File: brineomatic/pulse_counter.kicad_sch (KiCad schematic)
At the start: 6 parts, among them J1 Conn_01x03

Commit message: starting to shape up, footprints etc
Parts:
- C2: footprint (none) -> Capacitor_SMD:C_0805_2012Metric_Pad1.18x1.45mm_HandSolder
- J2: renamed from J1; footprint (none) -> TerminalBlock_Phoenix:TerminalBlock_Phoenix_PT-1,5-3-3.5-H_1x03_P3.50mm_Horizontal
- R5: renamed from R4; footprint (none) -> Resistor_SMD:R_0805_2012Metric_Pad1.20x1.40mm_HandSolder
- R6: renamed from R5; footprint (none) -> Resistor_SMD:R_0805_2012Metric_Pad1.20x1.40mm_HandSolder
- R7: renamed from R3; footprint (none) -> Resistor_SMD:R_0805_2012Metric_Pad1.20x1.40mm_HandSolder
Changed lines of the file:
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@@
 		(dnp no)
 		(fields_autoplaced yes)
-		(property "Reference" "#PWR04"
+		(property "Reference" "#PWR010"
 			(at 105.41 120.65 0)
 			(effects
@@
 			(project ""
 				(path "/96477ae2-ef08-48f3-8dd4-fe4478541f68/afb25a63-7dc0-4ba4-a0ca-4f0b83c59f3b"
-					(reference "#PWR04")
+					(reference "#PWR010")
 					(unit 1)
 				)
@@
 		(dnp no)
 		(fields_autoplaced yes)
-		(property "Reference" "#PWR03"
+		(property "Reference" "#PWR09"
 			(at 105.41 97.79 0)
 			(effects
@@
 			(project ""
 				(path "/96477ae2-ef08-48f3-8dd4-fe4478541f68/afb25a63-7dc0-4ba4-a0ca-4f0b83c59f3b"
-					(reference "#PWR03")
+					(reference "#PWR09")
 					(unit 1)
 				)
@@
 		(on_board yes)
 		(dnp no)
-		(property "Reference" "R3"
+		(property "Reference" "R7"
 			(at 135.89 99.06 90)
 			(effects
@@
 			)
 		)
-		(property "Footprint" ""
+		(property "Footprint" "Resistor_SMD:R_0805_2012Metric_Pad1.20x1.40mm_HandSolder"
 			(at 135.89 104.14 0)
 			(effects
@@
 			(project ""
 				(path "/96477ae2-ef08-48f3-8dd4-fe4478541f68/afb25a63-7dc0-4ba4-a0ca-4f0b83c59f3b"
-					(reference "R3")
+					(reference "R7")
 					(unit 1)
 				)
@@
 		(dnp no)
 		(fields_autoplaced yes)
-		(property "Reference" "J1"
+		(property "Reference" "J2"
 			(at 100.33 95.25 0)
 			(effects
@@
 			)
 		)
-		(property "Footprint" ""
+		(property "Footprint" "TerminalBlock_Phoenix:TerminalBlock_Phoenix_PT-1,5-3-3.5-H_1x03_P3.50mm_Horizontal"
 			(at 100.33 104.14 0)
 			(effects
@@
 			(project ""
 				(path "/96477ae2-ef08-48f3-8dd4-fe4478541f68/afb25a63-7dc0-4ba4-a0ca-4f0b83c59f3b"
-					(reference "J1")
+					(reference "J2")
 					(unit 1)
 				)
@@
 		(dnp no)
 		(fields_autoplaced yes)
-		(property "Reference" "R4"
+		(property "Reference" "R5"
 			(at 125.73 99.0599 0)
 			(effects
@@
 			)
 		)
-		(property "Footprint" ""
+		(property "Footprint" "Resistor_SMD:R_0805_2012Metric_Pad1.20x1.40mm_HandSolder"
 			(at 123.19 100.33 0)
 			(effects
@@
 			(project "brineomatic"
 				(path "/96477ae2-ef08-48f3-8dd4-fe4478541f68/afb25a63-7dc0-4ba4-a0ca-4f0b83c59f3b"
-					(reference "R4")
+					(reference "R5")
 					(unit 1)
 				)
@@
 			)
 		)
-		(property "Footprint" ""
+		(property "Footprint" "Capacitor_SMD:C_0805_2012Metric_Pad1.18x1.45mm_HandSolder"
 			(at 142.24 107.95 0)
 			(effects
@@
 		(dnp no)
 		(fields_autoplaced yes)
-		(property "Reference" "R5"
+		(property "Reference" "R6"
 			(at 125.73 106.6799 0)
 			(effects
@@
 			)
 		)
-		(property "Footprint" ""
+		(property "Footprint" "Resistor_SMD:R_0805_2012Metric_Pad1.20x1.40mm_HandSolder"
 			(at 123.19 107.95 0)
 			(effects
@@
 			(project "brineomatic"
 				(path "/96477ae2-ef08-48f3-8dd4-fe4478541f68/afb25a63-7dc0-4ba4-a0ca-4f0b83c59f3b"
-					(reference "R5")
-					(unit 1)
-				)
+					(reference "R6")
+					(unit 1)
+				)

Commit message: starting to look good.
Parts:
- J2: value Conn_01x03 -> FLOWMETER; footprint TerminalBlock_Phoenix:TerminalBlock_Phoenix_PT-1,5-3-3.5-H_1x03_P3.50mm_Horizontal -> Connector_JST:JST_PH_S3B-PH-K_1x03_P2.00mm_Horizontal; LCSC (none) -> C7470117
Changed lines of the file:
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@@
 			)
 		)
-		(property "Value" "Conn_01x03"
+		(property "Value" "FLOWMETER"
 			(at 100.33 97.79 0)
 			(effects
@@
 			)
 		)
-		(property "Footprint" "TerminalBlock_Phoenix:TerminalBlock_Phoenix_PT-1,5-3-3.5-H_1x03_P3.50mm_Horizontal"
+		(property "Footprint" "Connector_JST:JST_PH_S3B-PH-K_1x03_P2.00mm_Horizontal"
 			(at 100.33 104.14 0)
 			(effects
@@
 			(at 100.33 104.14 0)
 			(effects
+				(font
+					(size 1.27 1.27)
+				)
+				(hide yes)
+			)
+		)
+		(property "LCSC" "C7470117"
+			(at 100.33 104.14 0)
+			(effects

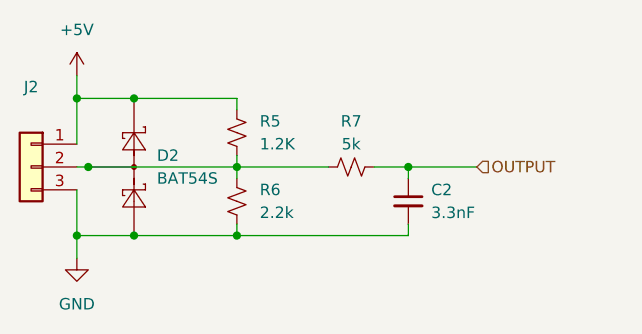
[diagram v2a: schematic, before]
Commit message: updated bom and prepping for Rev A
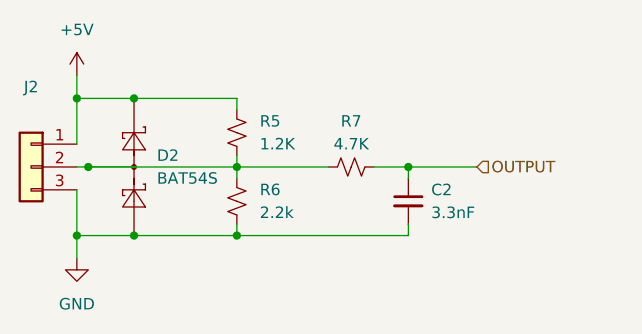
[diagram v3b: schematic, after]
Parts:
- C2: LCSC (none) -> C107149
- J2: value FLOWMETER -> ~; LCSC C7470117 -> C157929
- R5: LCSC (none) -> C114526
- R6: LCSC (none) -> C114561
- R7: value 5k -> 4.7K; LCSC (none) -> C60816
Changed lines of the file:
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@@
 			)
 		)
-		(property "Value" "5k"
+		(property "Value" "4.7K"
 			(at 135.89 101.6 90)
 			(effects
@@
 		)
 		(property "Description" "Resistor, small US symbol"
+			(at 135.89 104.14 0)
+			(effects
+				(font
+					(size 1.27 1.27)
+				)
+				(hide yes)
+			)
+		)
+		(property "LCSC" "C60816"
 			(at 135.89 104.14 0)
 			(effects
@@
 			)
 		)
-		(property "Value" "FLOWMETER"
+		(property "Value" "~"
 			(at 100.33 97.79 0)
 			(effects
@@
 			)
 		)
-		(property "LCSC" "C7470117"
+		(property "LCSC" "C157929"
 			(at 100.33 104.14 0)
 			(effects
@@
 			)
 		)
+		(property "LCSC" "C114526"
+			(at 123.19 100.33 0)
+			(effects
+				(font
+					(size 1.27 1.27)
+				)
+				(hide yes)
+			)
+		)
 		(pin "1"
 		)
@@
 			)
 		)
+		(property "LCSC" "C107149"
+			(at 142.24 107.95 0)
+			(effects
+				(font
+					(size 1.27 1.27)
+				)
+				(hide yes)
+			)
+		)
 		(pin "1"
 		)
@@
 			(at 123.19 107.95 0)
 			(effects
+				(font
+					(size 1.27 1.27)
+				)
+				(hide yes)
+			)
+		)
+		(property "LCSC" "C114561"
+			(at 123.19 107.95 0)
+			(effects

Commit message: fixed bat54s placement.
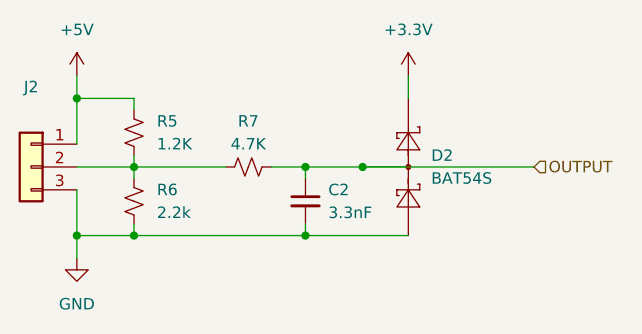
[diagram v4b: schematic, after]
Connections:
- net +5V: no longer D2.2 (K)
- net OUTPUT: now also D2.3 (COM)
- net at J2.2 (Pin_2), R5.1, R6.2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: no longer D2.3 (COM)
- new net +3.3V: D2.2 (K)
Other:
- moved on the sheet: C2, D2, R5, R6, R7

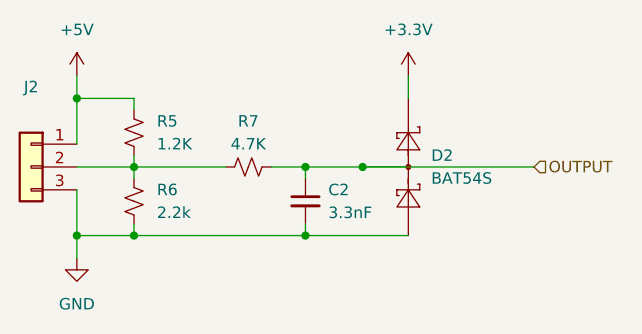
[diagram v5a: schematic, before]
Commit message: did a bunch of schematic work for Rev B
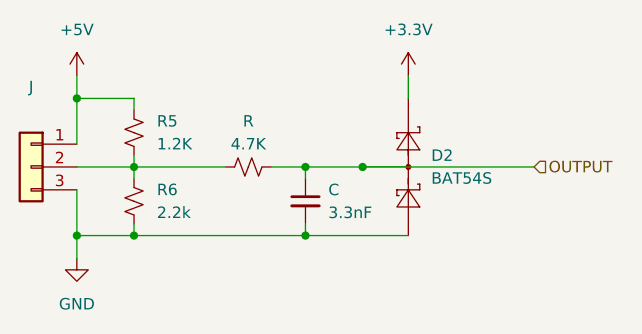
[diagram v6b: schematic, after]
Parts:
- renumbered C2 to C, J2 to J, R7 to R
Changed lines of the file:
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@@
 		(dnp no)
 		(fields_autoplaced yes)
-		(property "Reference" "#PWR010"
+		(property "Reference" "#PWR"
 			(at 105.41 120.65 0)
 			(effects
@@
 		)
 		(instances
-			(project ""
-				(path "/96477ae2-ef08-48f3-8dd4-fe4478541f68/afb25a63-7dc0-4ba4-a0ca-4f0b83c59f3b"
-					(reference "#PWR010")
+			(project "brineomatic"
+				(path "/96477ae2-ef08-48f3-8dd4-fe4478541f68/c28d9395-3f2f-46b5-bdab-c14b6c7c5c4b"
+					(reference "#PWR040")
 					(unit 1)
 				)
@@
 		(dnp no)
 		(fields_autoplaced yes)
-		(property "Reference" "#PWR027"
+		(property "Reference" "#PWR"
 			(at 142.24 97.79 0)
 			(effects
@@
 		)
 		(instances
-			(project ""
-				(path "/96477ae2-ef08-48f3-8dd4-fe4478541f68/afb25a63-7dc0-4ba4-a0ca-4f0b83c59f3b"
-					(reference "#PWR027")
+			(project "brineomatic"
+				(path "/96477ae2-ef08-48f3-8dd4-fe4478541f68/c28d9395-3f2f-46b5-bdab-c14b6c7c5c4b"
+					(reference "#PWR043")
 					(unit 1)
 				)
@@
 		(dnp no)
 		(fields_autoplaced yes)
-		(property "Reference" "#PWR09"
+		(property "Reference" "#PWR"
 			(at 105.41 97.79 0)
 			(effects
@@
 		)
 		(instances
-			(project ""
-				(path "/96477ae2-ef08-48f3-8dd4-fe4478541f68/afb25a63-7dc0-4ba4-a0ca-4f0b83c59f3b"
-					(reference "#PWR09")
+			(project "brineomatic"
+				(path "/96477ae2-ef08-48f3-8dd4-fe4478541f68/c28d9395-3f2f-46b5-bdab-c14b6c7c5c4b"
+					(reference "#PWR039")
 					(unit 1)
 				)
@@
 		(on_board yes)
 		(dnp no)
-		(property "Reference" "R7"
+		(property "Reference" "R"
 			(at 124.46 99.06 90)
 			(effects
@@
 		)
 		(instances
-			(project ""
-				(path "/96477ae2-ef08-48f3-8dd4-fe4478541f68/afb25a63-7dc0-4ba4-a0ca-4f0b83c59f3b"
-					(reference "R7")
+			(project "brineomatic"
+				(path "/96477ae2-ef08-48f3-8dd4-fe4478541f68/c28d9395-3f2f-46b5-bdab-c14b6c7c5c4b"
+					(reference "R14")
 					(unit 1)
 				)
@@
 		(dnp no)
 		(fields_autoplaced yes)
-		(property "Reference" "J2"
+		(property "Reference" "J"
 			(at 100.33 95.25 0)
 			(effects
@@
 		)
 		(instances
-			(project ""
-				(path "/96477ae2-ef08-48f3-8dd4-fe4478541f68/afb25a63-7dc0-4ba4-a0ca-4f0b83c59f3b"
-					(reference "J2")
+			(project "brineomatic"
+				(path "/96477ae2-ef08-48f3-8dd4-fe4478541f68/c28d9395-3f2f-46b5-bdab-c14b6c7c5c4b"
+					(reference "J20")
 					(unit 1)
 				)
@@
 					(unit 1)
 				)
+				(path "/96477ae2-ef08-48f3-8dd4-fe4478541f68/c28d9395-3f2f-46b5-bdab-c14b6c7c5c4b"
+					(reference "D11")
+					(unit 1)
+				)
 			)
 		)
@@
 					(unit 1)
 				)
+				(path "/96477ae2-ef08-48f3-8dd4-fe4478541f68/c28d9395-3f2f-46b5-bdab-c14b6c7c5c4b"
+					(reference "R9")
+					(unit 1)
+				)
 			)
 		)
@@
 		(dnp no)
 		(fields_autoplaced yes)
-		(property "Reference" "C2"
+		(property "Reference" "C"
 			(at 133.35 106.6862 0)
 			(effects
@@
 		)
 		(instances
-			(project ""
-				(path "/96477ae2-ef08-48f3-8dd4-fe4478541f68/afb25a63-7dc0-4ba4-a0ca-4f0b83c59f3b"
-					(reference "C2")
+			(project "brineomatic"
+				(path "/96477ae2-ef08-48f3-8dd4-fe4478541f68/c28d9395-3f2f-46b5-bdab-c14b6c7c5c4b"
+					(reference "C18")
 					(unit 1)
 				)
@@
 					(unit 1)
 				)
+				(path "/96477ae2-ef08-48f3-8dd4-fe4478541f68/c28d9395-3f2f-46b5-bdab-c14b6c7c5c4b"
+					(reference "R10")
+					(unit 1)
+				)

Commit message: worked on schematic and layout a bit more.
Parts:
- C9: renamed from C; footprint Capacitor_SMD:C_0805_2012Metric_Pad1.18x1.45mm_HandSolder -> Capacitor_SMD:C_0603_1608Metric
- R5, R6: footprint Resistor_SMD:R_0805_2012Metric_Pad1.20x1.40mm_HandSolder -> Resistor_SMD:R_0603_1608Metric
- R7: renamed from R; footprint Resistor_SMD:R_0805_2012Metric_Pad1.20x1.40mm_HandSolder -> Resistor_SMD:R_0603_1608Metric
- renumbered J to J2
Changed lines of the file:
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@@
 		(dnp no)
 		(fields_autoplaced yes)
-		(property "Reference" "#PWR"
+		(property "Reference" "#PWR0101"
 			(at 105.41 120.65 0)
 			(effects
@@
 		(instances
 			(project "brineomatic"
+				(path "/96477ae2-ef08-48f3-8dd4-fe4478541f68/afb25a63-7dc0-4ba4-a0ca-4f0b83c59f3b"
+					(reference "#PWR0101")
+					(unit 1)
+				)
 				(path "/96477ae2-ef08-48f3-8dd4-fe4478541f68/c28d9395-3f2f-46b5-bdab-c14b6c7c5c4b"
 					(reference "#PWR040")
@@
 		(dnp no)
 		(fields_autoplaced yes)
-		(property "Reference" "#PWR"
+		(property "Reference" "#PWR0103"
 			(at 142.24 97.79 0)
 			(effects
@@
 		(instances
 			(project "brineomatic"
+				(path "/96477ae2-ef08-48f3-8dd4-fe4478541f68/afb25a63-7dc0-4ba4-a0ca-4f0b83c59f3b"
+					(reference "#PWR0103")
+					(unit 1)
+				)
 				(path "/96477ae2-ef08-48f3-8dd4-fe4478541f68/c28d9395-3f2f-46b5-bdab-c14b6c7c5c4b"
 					(reference "#PWR043")
@@
 		(dnp no)
 		(fields_autoplaced yes)
-		(property "Reference" "#PWR"
+		(property "Reference" "#PWR0102"
 			(at 105.41 97.79 0)
 			(effects
@@
 		(instances
 			(project "brineomatic"
+				(path "/96477ae2-ef08-48f3-8dd4-fe4478541f68/afb25a63-7dc0-4ba4-a0ca-4f0b83c59f3b"
+					(reference "#PWR0102")
+					(unit 1)
+				)
 				(path "/96477ae2-ef08-48f3-8dd4-fe4478541f68/c28d9395-3f2f-46b5-bdab-c14b6c7c5c4b"
 					(reference "#PWR039")
@@
 		(on_board yes)
 		(dnp no)
-		(property "Reference" "R"
+		(property "Reference" "R7"
 			(at 124.46 99.06 90)
 			(effects
@@
 			)
 		)
-		(property "Footprint" "Resistor_SMD:R_0805_2012Metric_Pad1.20x1.40mm_HandSolder"
+		(property "Footprint" "Resistor_SMD:R_0603_1608Metric"
 			(at 124.46 104.14 0)
 			(effects
@@
 		(instances
 			(project "brineomatic"
+				(path "/96477ae2-ef08-48f3-8dd4-fe4478541f68/afb25a63-7dc0-4ba4-a0ca-4f0b83c59f3b"
+					(reference "R7")
+					(unit 1)
+				)
 				(path "/96477ae2-ef08-48f3-8dd4-fe4478541f68/c28d9395-3f2f-46b5-bdab-c14b6c7c5c4b"
 					(reference "R14")
@@
 		(dnp no)
 		(fields_autoplaced yes)
-		(property "Reference" "J"
+		(property "Reference" "J2"
 			(at 100.33 95.25 0)
 			(effects
@@
 		(instances
 			(project "brineomatic"
+				(path "/96477ae2-ef08-48f3-8dd4-fe4478541f68/afb25a63-7dc0-4ba4-a0ca-4f0b83c59f3b"
+					(reference "J2")
+					(unit 1)
+				)
 				(path "/96477ae2-ef08-48f3-8dd4-fe4478541f68/c28d9395-3f2f-46b5-bdab-c14b6c7c5c4b"
 					(reference "J20")
@@
 			)
 		)
-		(property "Footprint" "Resistor_SMD:R_0805_2012Metric_Pad1.20x1.40mm_HandSolder"
+		(property "Footprint" "Resistor_SMD:R_0603_1608Metric"
 			(at 111.76 100.33 0)
 			(effects
@@
 		(dnp no)
 		(fields_autoplaced yes)
-		(property "Reference" "C"
+		(property "Reference" "C9"
 			(at 133.35 106.6862 0)
 			(effects
@@
 			)
 		)
-		(property "Footprint" "Capacitor_SMD:C_0805_2012Metric_Pad1.18x1.45mm_HandSolder"
+		(property "Footprint" "Capacitor_SMD:C_0603_1608Metric"
 			(at 130.81 107.95 0)
 			(effects
@@
 		(instances
 			(project "brineomatic"
+				(path "/96477ae2-ef08-48f3-8dd4-fe4478541f68/afb25a63-7dc0-4ba4-a0ca-4f0b83c59f3b"
+					(reference "C9")
+					(unit 1)
+				)
 				(path "/96477ae2-ef08-48f3-8dd4-fe4478541f68/c28d9395-3f2f-46b5-bdab-c14b6c7c5c4b"
 					(reference "C18")
@@
 			)
 		)
-		(property "Footprint" "Resistor_SMD:R_0805_2012Metric_Pad1.20x1.40mm_HandSolder"
+		(property "Footprint" "Resistor_SMD:R_0603_1608Metric"
 			(at 111.76 107.95 0)
 			(effects

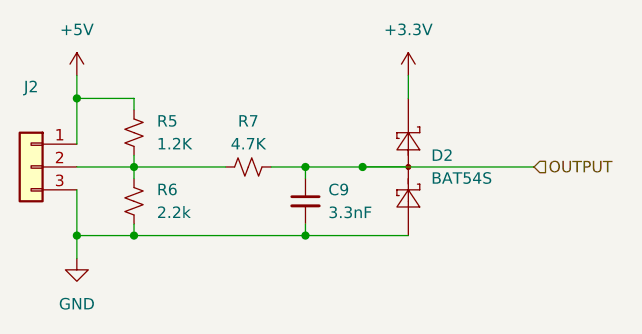
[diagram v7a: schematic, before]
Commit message: tmc2209 driver schematic checked and laid out nicely.
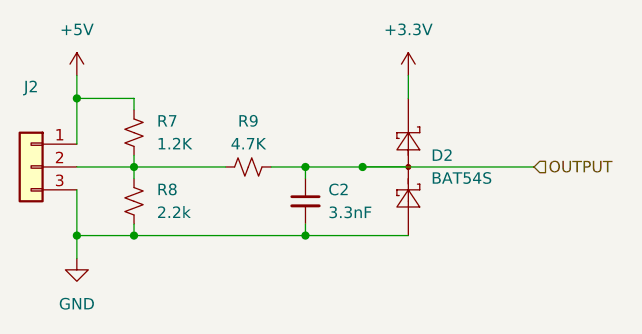
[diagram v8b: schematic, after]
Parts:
- renumbered C9 to C2, R5 to R7, R6 to R8, R7 to R9
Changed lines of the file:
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@@
 		(dnp no)
 		(fields_autoplaced yes)
-		(property "Reference" "#PWR0101"
+		(property "Reference" "#PWR011"
 			(at 105.41 120.65 0)
 			(effects
@@
 			(project "brineomatic"
 				(path "/96477ae2-ef08-48f3-8dd4-fe4478541f68/afb25a63-7dc0-4ba4-a0ca-4f0b83c59f3b"
-					(reference "#PWR0101")
-					(unit 1)
-				)
-				(path "/96477ae2-ef08-48f3-8dd4-fe4478541f68/c28d9395-3f2f-46b5-bdab-c14b6c7c5c4b"
-					(reference "#PWR040")
+					(reference "#PWR011")
+					(unit 1)
+				)
+				(path "/96477ae2-ef08-48f3-8dd4-fe4478541f68/c28d9395-3f2f-46b5-bdab-c14b6c7c5c4b"
+					(reference "#PWR031")
 					(unit 1)
 				)
@@
 		(dnp no)
 		(fields_autoplaced yes)
-		(property "Reference" "#PWR0103"
+		(property "Reference" "#PWR012"
 			(at 142.24 97.79 0)
 			(effects
@@
 			(project "brineomatic"
 				(path "/96477ae2-ef08-48f3-8dd4-fe4478541f68/afb25a63-7dc0-4ba4-a0ca-4f0b83c59f3b"
-					(reference "#PWR0103")
-					(unit 1)
-				)
-				(path "/96477ae2-ef08-48f3-8dd4-fe4478541f68/c28d9395-3f2f-46b5-bdab-c14b6c7c5c4b"
-					(reference "#PWR043")
+					(reference "#PWR012")
+					(unit 1)
+				)
+				(path "/96477ae2-ef08-48f3-8dd4-fe4478541f68/c28d9395-3f2f-46b5-bdab-c14b6c7c5c4b"
+					(reference "#PWR032")
 					(unit 1)
 				)
@@
 		(dnp no)
 		(fields_autoplaced yes)
-		(property "Reference" "#PWR0102"
+		(property "Reference" "#PWR010"
 			(at 105.41 97.79 0)
 			(effects
@@
 			(project "brineomatic"
 				(path "/96477ae2-ef08-48f3-8dd4-fe4478541f68/afb25a63-7dc0-4ba4-a0ca-4f0b83c59f3b"
-					(reference "#PWR0102")
-					(unit 1)
-				)
-				(path "/96477ae2-ef08-48f3-8dd4-fe4478541f68/c28d9395-3f2f-46b5-bdab-c14b6c7c5c4b"
-					(reference "#PWR039")
+					(reference "#PWR010")
+					(unit 1)
+				)
+				(path "/96477ae2-ef08-48f3-8dd4-fe4478541f68/c28d9395-3f2f-46b5-bdab-c14b6c7c5c4b"
+					(reference "#PWR030")
 					(unit 1)
 				)
@@
 		(on_board yes)
 		(dnp no)
-		(property "Reference" "R7"
+		(property "Reference" "R9"
 			(at 124.46 99.06 90)
 			(effects
@@
 			(project "brineomatic"
 				(path "/96477ae2-ef08-48f3-8dd4-fe4478541f68/afb25a63-7dc0-4ba4-a0ca-4f0b83c59f3b"
-					(reference "R7")
-					(unit 1)
-				)
-				(path "/96477ae2-ef08-48f3-8dd4-fe4478541f68/c28d9395-3f2f-46b5-bdab-c14b6c7c5c4b"
-					(reference "R14")
+					(reference "R9")
+					(unit 1)
+				)
+				(path "/96477ae2-ef08-48f3-8dd4-fe4478541f68/c28d9395-3f2f-46b5-bdab-c14b6c7c5c4b"
+					(reference "R23")
 					(unit 1)
 				)
@@
 				)
 				(path "/96477ae2-ef08-48f3-8dd4-fe4478541f68/c28d9395-3f2f-46b5-bdab-c14b6c7c5c4b"
-					(reference "J20")
+					(reference "J10")
 					(unit 1)
 				)
@@
 				)
 				(path "/96477ae2-ef08-48f3-8dd4-fe4478541f68/c28d9395-3f2f-46b5-bdab-c14b6c7c5c4b"
-					(reference "D11")
+					(reference "D12")
 					(unit 1)
 				)
@@
 		(dnp no)
 		(fields_autoplaced yes)
-		(property "Reference" "R5"
+		(property "Reference" "R7"
 			(at 114.3 99.0599 0)
 			(effects
@@
 			(project "brineomatic"
 				(path "/96477ae2-ef08-48f3-8dd4-fe4478541f68/afb25a63-7dc0-4ba4-a0ca-4f0b83c59f3b"
-					(reference "R5")
-					(unit 1)
-				)
-				(path "/96477ae2-ef08-48f3-8dd4-fe4478541f68/c28d9395-3f2f-46b5-bdab-c14b6c7c5c4b"
-					(reference "R9")
+					(reference "R7")
+					(unit 1)
+				)
+				(path "/96477ae2-ef08-48f3-8dd4-fe4478541f68/c28d9395-3f2f-46b5-bdab-c14b6c7c5c4b"
+					(reference "R21")
 					(unit 1)
 				)
@@
 		(dnp no)
 		(fields_autoplaced yes)
-		(property "Reference" "C9"
+		(property "Reference" "C2"
 			(at 133.35 106.6862 0)
 			(effects
@@
 			(project "brineomatic"
 				(path "/96477ae2-ef08-48f3-8dd4-fe4478541f68/afb25a63-7dc0-4ba4-a0ca-4f0b83c59f3b"
-					(reference "C9")
-					(unit 1)
-				)
-				(path "/96477ae2-ef08-48f3-8dd4-fe4478541f68/c28d9395-3f2f-46b5-bdab-c14b6c7c5c4b"
-					(reference "C18")
+					(reference "C2")
+					(unit 1)
+				)
+				(path "/96477ae2-ef08-48f3-8dd4-fe4478541f68/c28d9395-3f2f-46b5-bdab-c14b6c7c5c4b"
+					(reference "C13")
 					(unit 1)
 				)
@@
 		(dnp no)
 		(fields_autoplaced yes)
-		(property "Reference" "R6"
+		(property "Reference" "R8"
 			(at 114.3 106.6799 0)
 			(effects
@@
 			(project "brineomatic"
 				(path "/96477ae2-ef08-48f3-8dd4-fe4478541f68/afb25a63-7dc0-4ba4-a0ca-4f0b83c59f3b"
-					(reference "R6")
-					(unit 1)
-				)
-				(path "/96477ae2-ef08-48f3-8dd4-fe4478541f68/c28d9395-3f2f-46b5-bdab-c14b6c7c5c4b"
-					(reference "R10")
-					(unit 1)
-				)
+					(reference "R8")
+					(unit 1)
+				)
+				(path "/96477ae2-ef08-48f3-8dd4-fe4478541f68/c28d9395-3f2f-46b5-bdab-c14b6c7c5c4b"
+					(reference "R22")
+					(unit 1)
+				)
